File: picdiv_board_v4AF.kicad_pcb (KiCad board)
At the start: 2 copper layers, 100 x 99.5 mm, 77 parts, among them J1 DC-Input, J10 PPS_B, J11 PPS_B, J2 MountingHole_M2.5, J3 MountingHole_M2.5, J4 TEST_1PPS, J5 Conn_01x06, J6 Sync, J7 Sync, J8 10MHz, J9 10MHz, SW1 SW_DIP_x03, U1 LT1963AxST-3.3, U2 LT1963AxST-3.3, U3 PIC12F675-xSN, U4 LTC6993xS6-1, U5 IDT5PB1108, U6 IDT5PB1108, U7 LT1963AEQ, U8 ADR4540

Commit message: Create AN2093.pdf
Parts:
- moved C24 0.50 mm to (161.0, 86.5)
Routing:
- net +5V: track 54.2 -> 65.6 mm, vias 0 -> 1
- net GND: vias 140 -> 135
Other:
- board text removed: "PPS-board 2019.01 (rev3) https://github.com/aewallin/PICDIV_Board_v3 Licensed under CERN OHL v.1.2 or later http://ohwr.org/cernohl Anders Wallin 2018-07-12"
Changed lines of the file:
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@@
 	(footprint "Capacitor_SMD:C_0402_1005Metric_Pad0.74x0.62mm_HandSolder"
 		(layer "F.Cu")
-		(at 161 86)
+		(at 161 86.5)
 		(descr "Capacitor SMD 0402 (1005 Metric), square (rectangular) end terminal, IPC_7351 nominal with elongated pad for handsoldering. (Body size source: IPC-SM-782 page 76, https://www.pcb-3d.com/wordpress/wp-content/uploads/ipc-sm-782a_amendment_1_and_2.pdf), generated with kicad-footprint-generator")
 		(tags "capacitor handsolder")
@@
 		)
 	)
-	(gr_text "PPS-board 2019.01 (rev3)\nhttps://github.com/aewallin/PICDIV_Board_v3\nLicensed under CERN OHL v.1.2 or later\nhttp://ohwr.org/cernohl\nAnders Wallin 2018-07-12"
-		(at 152 109.3 90)
-		(layer "F.SilkS")
-		(effects
-			(font
-				(size 1 1)
-				(thickness 0.25)
-			)
-			(justify left)
-		)
-	)
 	(gr_text "+V"
 		(at 218.8 70 0)
@@
 	)
 	(via
-		(at 162.3 91.2)
-		(size 0.7)
-		(drill 0.4)
-		(layers "F.Cu" "B.Cu")
-		(free yes)
-		(net 2)
-	)
-	(via
 		(at 195 135)
 		(size 0.7)
@@
 	)
 	(via
-		(at 160 76)
-		(size 0.7)
-		(drill 0.4)
-		(layers "F.Cu" "B.Cu")
-		(net 2)
-	)
-	(via
 		(at 140 131)
 		(size 0.7)
@@
 	)
 	(via
-		(at 162.9 86)
+		(at 163.2 86.5)
 		(size 0.7)
 		(drill 0.4)
@@
 	)
 	(via
-		(at 164 82)
-		(size 0.7)
-		(drill 0.4)
-		(layers "F.Cu" "B.Cu")
-		(net 2)
-	)
-	(via
 		(at 153.5 115.5)
 		(size 0.7)
@@
 	)
 	(via
-		(at 160 65)
-		(size 0.7)
-		(drill 0.4)
-		(layers "F.Cu" "B.Cu")
-		(net 2)
-	)
-	(via
 		(at 140 80)
 		(size 0.7)
@@
 	)
 	(via
-		(at 160 70)
-		(size 0.7)
-		(drill 0.4)
-		(layers "F.Cu" "B.Cu")
-		(net 2)
-	)
-	(via
 		(at 153 137)
 		(size 0.7)
@@
 		(start 160.475 81.525)
 		(end 160.475 88.425)
+		(width 0.7)
+		(layer "F.Cu")
+		(net 5)
+	)
+	(segment
+		(start 161 91)
+		(end 160.4 90.4)
 		(width 0.8)
 		(layer "F.Cu")
@@
 	)
 	(segment
-		(start 165 77)
-		(end 160.475 81.525)
+		(start 160.4 90.4)
+		(end 160.4 88.5)
+		(width 0.8)
+		(layer "F.Cu")
+		(net 5)
+	)
+	(via
+		(at 161 91)
+		(size 0.7)
+		(drill 0.4)
+		(layers "F.Cu" "B.Cu")
+		(net 5)
+	)
+	(segment
+		(start 186 87)
+		(end 182 91)
+		(width 0.8)
+		(layer "B.Cu")
+		(net 5)
+	)
+	(segment
+		(start 182 91)
+		(end 161 91)
 		(width 0.8)
 		(layer "B.Cu")
@@
 	(segment
 		(start 188.5 77)
-		(end 165 77)
+		(end 187 77)
+		(width 0.8)
+		(layer "B.Cu")
+		(net 5)
+	)
+	(segment
+		(start 186 78)
+		(end 186 87)
+		(width 0.8)
+		(layer "B.Cu")
+		(net 5)
+	)
+	(segment
+		(start 187 77)
+		(end 186 78)
 		(width 0.8)
 		(layer "B.Cu")
@@
 			)
 		)
+	)
+	(zone
+		(net 0)
+		(net_name "")
+		(layers "F&B.Cu")
+		(name "Thermal Isolation")
+		(hatch edge 0.5)
+		(connect_pads
+			(clearance 0)
+		)
+		(min_thickness 0.25)
+		(filled_areas_thickness no)
+		(keepout
+			(tracks allowed)
+			(vias allowed)
+			(pads allowed)
+			(copperpour not_allowed)
+			(footprints allowed)
+		)
+		(fill
+			(thermal_gap 0.5)
+			(thermal_bridge_width 0.5)
+		)
+		(polygon
+			(pts
+				(xy 156 58) (xy 156 86) (xy 184 86) (xy 184 58)
+			)
+		)

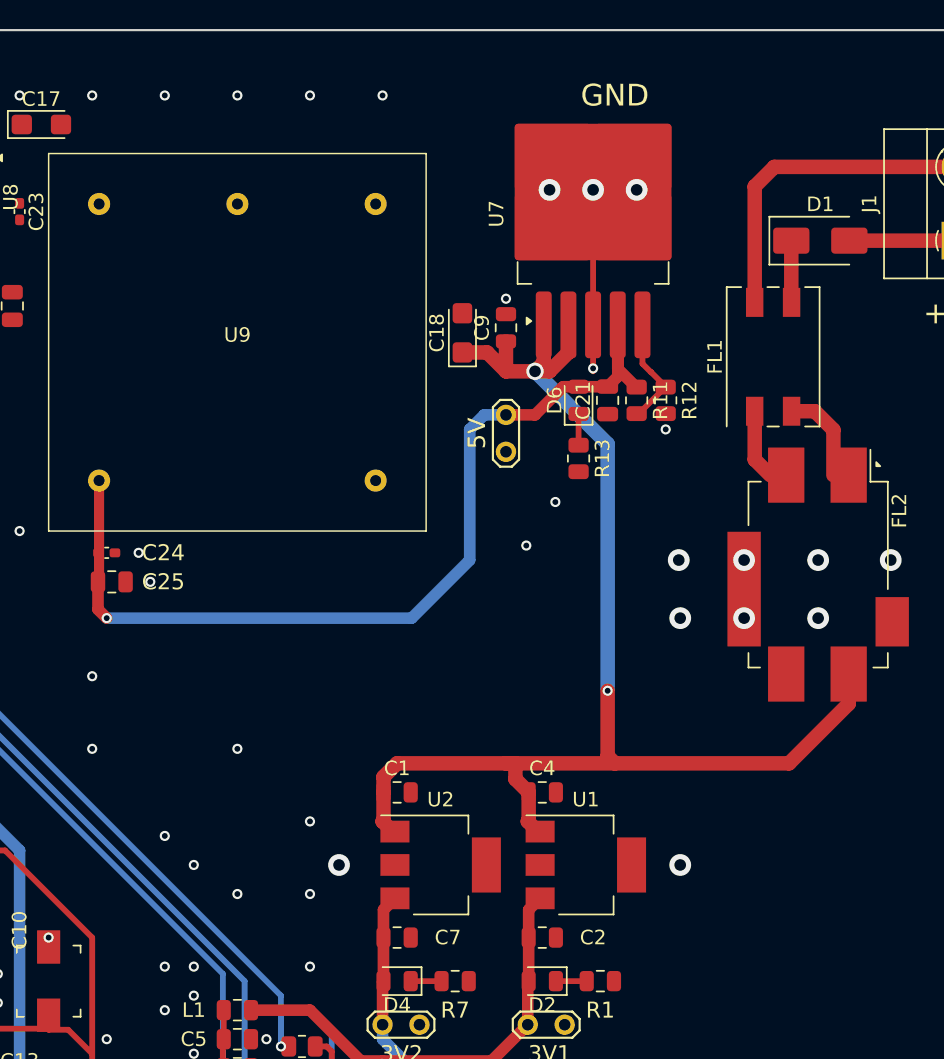
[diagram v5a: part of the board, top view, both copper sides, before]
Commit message: Layout
Better Vias.   Rotate OCXO.   Lots of cleanup.  Lots more work needed.
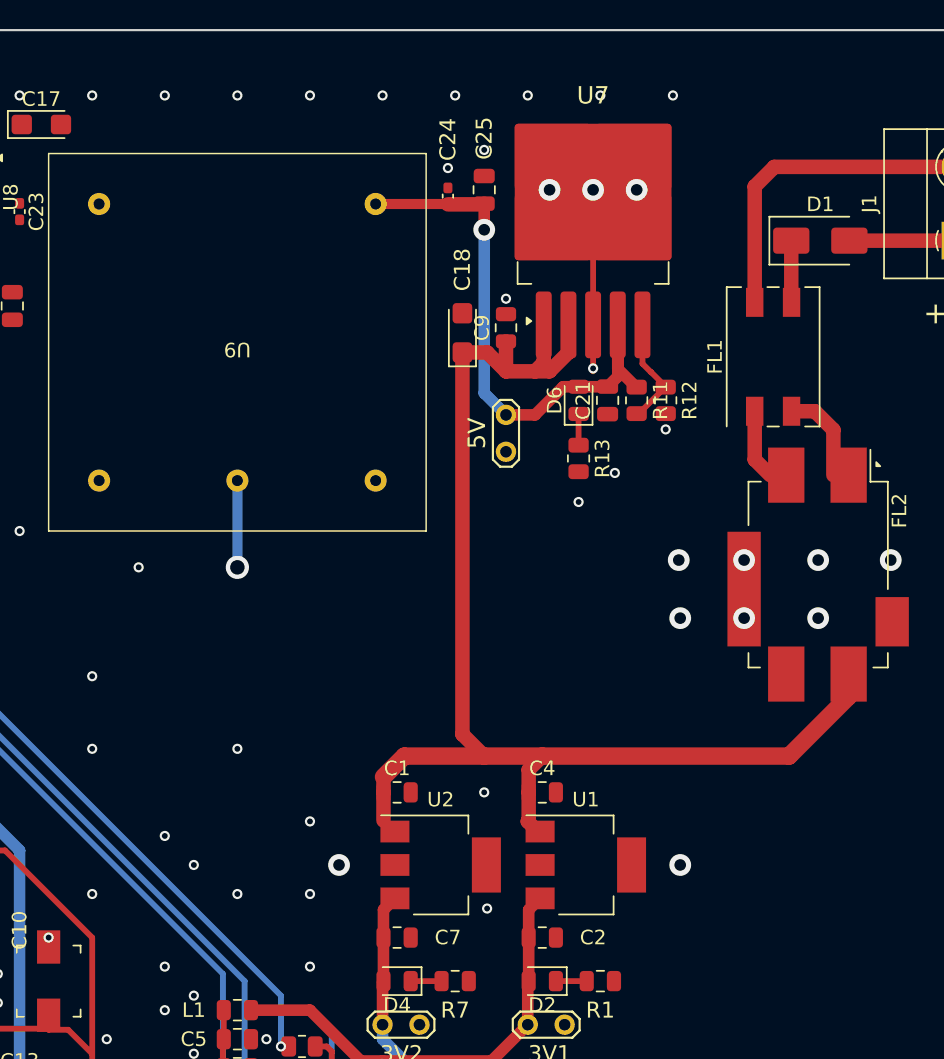
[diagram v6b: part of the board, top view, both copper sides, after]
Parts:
- moved C25 37.2 mm to (187.0, 61.5), turned to 90 degrees
- moved C24 34.0 mm to (184.5, 61.9), turned to 90 degrees
- turned U9 to 180 degrees
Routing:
- net +5V: track 65.6 -> 39.9 mm
- net GND: track 55.3 -> 61.3 mm, vias 135 -> 143
- net LDO_IN: track 91.7 -> 89.3 mm, vias 2 -> 0
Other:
- board text removed: "GND"

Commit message: layout
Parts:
- added C26: 100nF, Capacitor_SMD:C_0402_1005Metric_Pad0.74x0.62mm_HandSolder, F.Cu at (178.0, 97.5)
- 2V1: value TEST_VADJ -> VADJ
- U1, U2: value LT1963AxST-3.3 -> LT1963AEST-3.3
- moved C19 28.3 mm to (178.0, 66.0), turned to 90 degrees
- moved C17 24.9 mm to (180.1, 65.0), turned to 90 degrees
- moved C25 21.1 mm to (165.9, 61.0)
- moved C24 12.5 mm to (172.5, 58.5)
- moved U9 9.62 mm to (168.5, 81.5)

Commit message: More layout, mostly around Vadg
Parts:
- removed C26: 100nF, Capacitor_SMD:C_0402_1005Metric_Pad0.74x0.62mm_HandSolder
- C20: renamed from C21; value 10u -> 10µF
- moved 2V1 46.6 mm to (173.0, 99.2), turned to 90 degrees
- moved C23 41.4 mm to (177.9, 97.5), turned to 0 degrees
- moved C24 24.0 mm to (153.0, 72.4)
- moved RN1 16.7 mm to (134.6, 71.0), turned to -90 degrees
- moved C22 14.6 mm to (140.0, 70.8)
- moved C21 13.8 mm to (137.6, 71.2), turned to 90 degrees
- moved U8 11.2 mm to (147.8, 72.7), turned to 180 degrees
- moved R9 2.00 mm to (142.0, 84.0)
- renumbered C20 to C21
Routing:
- net Net-(J6-In): track 0.00 -> 13.0 mm
- net Net-(RN1-R1.2): track 0.00 -> 4.17 mm
- net Net-(RN1-R3.2): track 0.00 -> 0.87 mm
- net GND: vias 143 -> 139
